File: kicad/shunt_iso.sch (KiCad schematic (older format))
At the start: 78 parts

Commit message: Come back to moldova to finish schematics and begin layout
I've started again from Moldova to discuss with Alexander the details.
I'm now working with schematics requeriments.
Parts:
- removed R?: 1M, symbol servo:Resistor
- added C? (x6): 100nF, symbol servo:Capacitor
- added C? (x2): 330p, symbol servo:Capacitor
- added J? (x2): Screw_Terminal_01x03, symbol Connector:Screw_Terminal_01x03
- added R? (x4): 1k, symbol servo:Resistor
- added R? (x4): 12e, symbol servo:Resistor
- added R?: 1M, symbol servo:Resistor
- added U? (x2): AMC1301, symbol servo:AMC1301
- added U? (x2): RFM-0505S, Converter_DCDC:C, symbol servo:RFM-0505S
- U: renamed from U?; value AMC1100 -> AMC1301; symbol servo:AMC1100 -> servo:AMC1301
- U?: value AMC1100 -> AMC1301; symbol servo:AMC1100 -> servo:AMC1301
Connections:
- net labels added: SHUNT_ISOA_ALLN, SHUNT_ISOA_ALLP, SHUNT_ISOB_ALLN, SHUNT_ISOB_ALLP
- wire segments 281 -> 361
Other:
- note added: "All"
- note added: "Measurement of A/B motor \nUVW phase current and A/B\nsum current, plus Vbus voltage"
- note added: "U"
- note added: "V"
- note added: "Vbus"
- note added: "W"
- note added: "with 3 screw connector you could choose\n3 range of current measurement to be at \n0.25v scale 1x, 2x or 4x.\n1-3 ------- X\n1-2 or 2-3 ------- 2X\n1-2 and 1-3 ------- 4X"
- moved on the sheet: C?, J?, R?, U?

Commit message: I've decided LEM lxs series, it's the best..
I've decided to use the LEM lxs, is a new series better than LTS and is
pin to pin compatible with the old one and also CAS series, so I think
it's a good option. 0.5usec rise time, multi prymari turns options, and
so..
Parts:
- removed C? (x20): 100nF, symbol servo:Capacitor
- removed C? (x4): 330p, symbol servo:Capacitor
- removed J? (x4): Screw_Terminal_01x03, symbol Connector:Screw_Terminal_01x03
- removed R? (x2): 1k, symbol servo:Resistor
- removed R? (x8): 12e, symbol servo:Resistor
- removed R? (x6): 20m, symbol servo:Resistor
- removed U (x3), U?: AMC1301, symbol servo:AMC1301
- removed U? (x8): RFM-0505S, Converter_DCDC:C, symbol servo:RFM-0505S
- added C? (x20): 100nF, symbol servo:Capacitor
- added C? (x9): 100n, symbol servo:C_Small
- added C? (x4): 330p, symbol servo:Capacitor
- added J? (x4): Screw_Terminal_01x03, symbol Connector:Screw_Terminal_01x03
- added L? (x18): L_Small, symbol servo:L_Small
- added R? (x18): 1k, symbol Device:R_Small
- added R? (x6): 20m, symbol servo:Resistor
- added R? (x8): 12e, symbol servo:Resistor
- added R? (x2): 1k, symbol servo:Resistor
- added U? (x8): RFM-0505S, Converter_DCDC:C, symbol servo:RFM-0505S
- added U? (x4): AMC1301, symbol servo:AMC1301
- renumbered U to U?
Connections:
- net 3V3: now also C?.2, C?.2, C?.2, C?.2, U?.1 (VDD1), U?.8 (VDD2), U?.8 (VDD2), U?.8 (VDD2)
- net GND: now also C?.1, C?.1, C?.1, C?.1, U?.4 (GND1), U?.5 (GND2), U?.5 (GND2), U?.5 (GND2)
- net GNDH: now also C?.1, C?.1, C?.1, C?.1, C?.1, C?.1, C?.1, C?.1, U?.1 (-VIN), U?.1 (-VIN), U?.1 (-VIN), U?.1 (-VIN), U?.1 (-VIN), U?.1 (-VIN), U?.1 (-VIN), U?.1 (-VIN)
- net SHUNT_ISOA_ALLN: now also C?.2, R?.2; no longer U?.6 (VOUT_N)
- net SHUNT_ISOA_ALLP: now also C?.1, R?.2; no longer U?.7 (VOUT_P)
- net SHUNT_ISOA_UN: now also C?.2, R?.2; no longer U?.6 (VOUT_N)
- net SHUNT_ISOA_UP: now also C?.1, R?.2; no longer U?.7 (VOUT_P)
- net SHUNT_ISOA_VN: now also C?.2, R?.2; no longer U?.6 (VOUT_N)
- net SHUNT_ISOA_VP: now also C?.1, R?.2; no longer U?.7 (VOUT_P)
- net SHUNT_ISOA_WN: now also C?.2, R?.2; no longer U?.3 (VIN_N)
- net SHUNT_ISOA_WP: now also C?.1, R?.2; no longer U?.2 (VIN_P)
- net SHUNT_ISOB_ALLN: now also C?.2, R?.2
- net SHUNT_ISOB_ALLP: now also C?.1, R?.2
- net SHUNT_ISOB_UN: now also C?.2, R?.2
- net SHUNT_ISOB_UP: now also C?.1, R?.2
- net SHUNT_ISOB_VN: now also C?.2, R?.2
- net SHUNT_ISOB_VP: now also C?.1, R?.2
- net SHUNT_ISOB_WN: now also C?.2, R?.2
- net SHUNT_ISOB_WP: now also C?.1, R?.2
- net SHUNT_ISO_BUSN: now also C?.2, R?.2; no longer U?.6 (VOUT_N)
- net SHUNT_ISO_BUSP: now also C?.1, R?.2; no longer U?.7 (VOUT_P)
- net at C?.2, U?.1 (VDD1): now also L?.1; no longer U?.4 (+VOUT)
- net at U?.1 (VDD1): now also C?.2, L?.1 (x3)
- net at C?.1, R?.1, U?.3 (VIN_N)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: now also C?.1, U?.3 (-VOUT) (x3)
- net at C?.1, R?.1, U?.5 (GND2)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: now also C?.1, U?.3 (-VOUT)
- net at U?.8 (VDD2): now also C?.2, L?.1
- net 15VH: no longer names the net of C?.2, U?.2 (+VIN)
- net 15VH: now also L?.2
- new net: R?.1, U?.6 (VOUT_N) (x7)
- new net: R?.1, U?.7 (VOUT_P) (x7)
- new net: L?.2, U?.4 (+VOUT) (x9)
- new net: R?.1, U?.2 (VIN_P) (x2)
- new net: R?.1, U?.3 (VIN_N) (x2)
- new net: C?.2, L?.2, U?.2 (+VIN) (x8)
- new net: C?.2, L?.1, U?.1 (VDD1) (x3)
- new net: C?.2, R?.1, U?.2 (VIN_P) (x3)
- new net: C?.1, C?.1, R?.1, U?.3 (-VOUT), U?.3 (VIN_N), U?.4 (GND1) (x3)
- new net: J?.2 (Pin_2), R?.1, R?.2 (x4)
- new net: J?.1 (Pin_1), R?.2, R?.2 (x4)
- new net: J?.3 (Pin_3), R?.1, R?.2 (x4)
- new net: C?.1, C?.1, R?.1, U?.3 (-VOUT), U?.5 (GND2), U?.6 (VOUT_N)
- new net: C?.2, R?.1, U?.7 (VOUT_P)
- new net: C?.2, L?.1, U?.8 (VDD2)
- new net 5VH: L?.1, L?.1, L?.1, L?.1, L?.1, L?.1, L?.1, L?.1, L?.1
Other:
- note added: "Current of 3 phases +\nsum current +\nVbus voltage"
- note added: "SHUT -> ADC -> SD -> DAC\n"
- note added: "divider to measure Vbus"
- note removed: "Measurement of A/B motor \nUVW phase current and A/B\nsum current, plus Vbus voltage"
- moved on the sheet: C?, J?, R?, U?

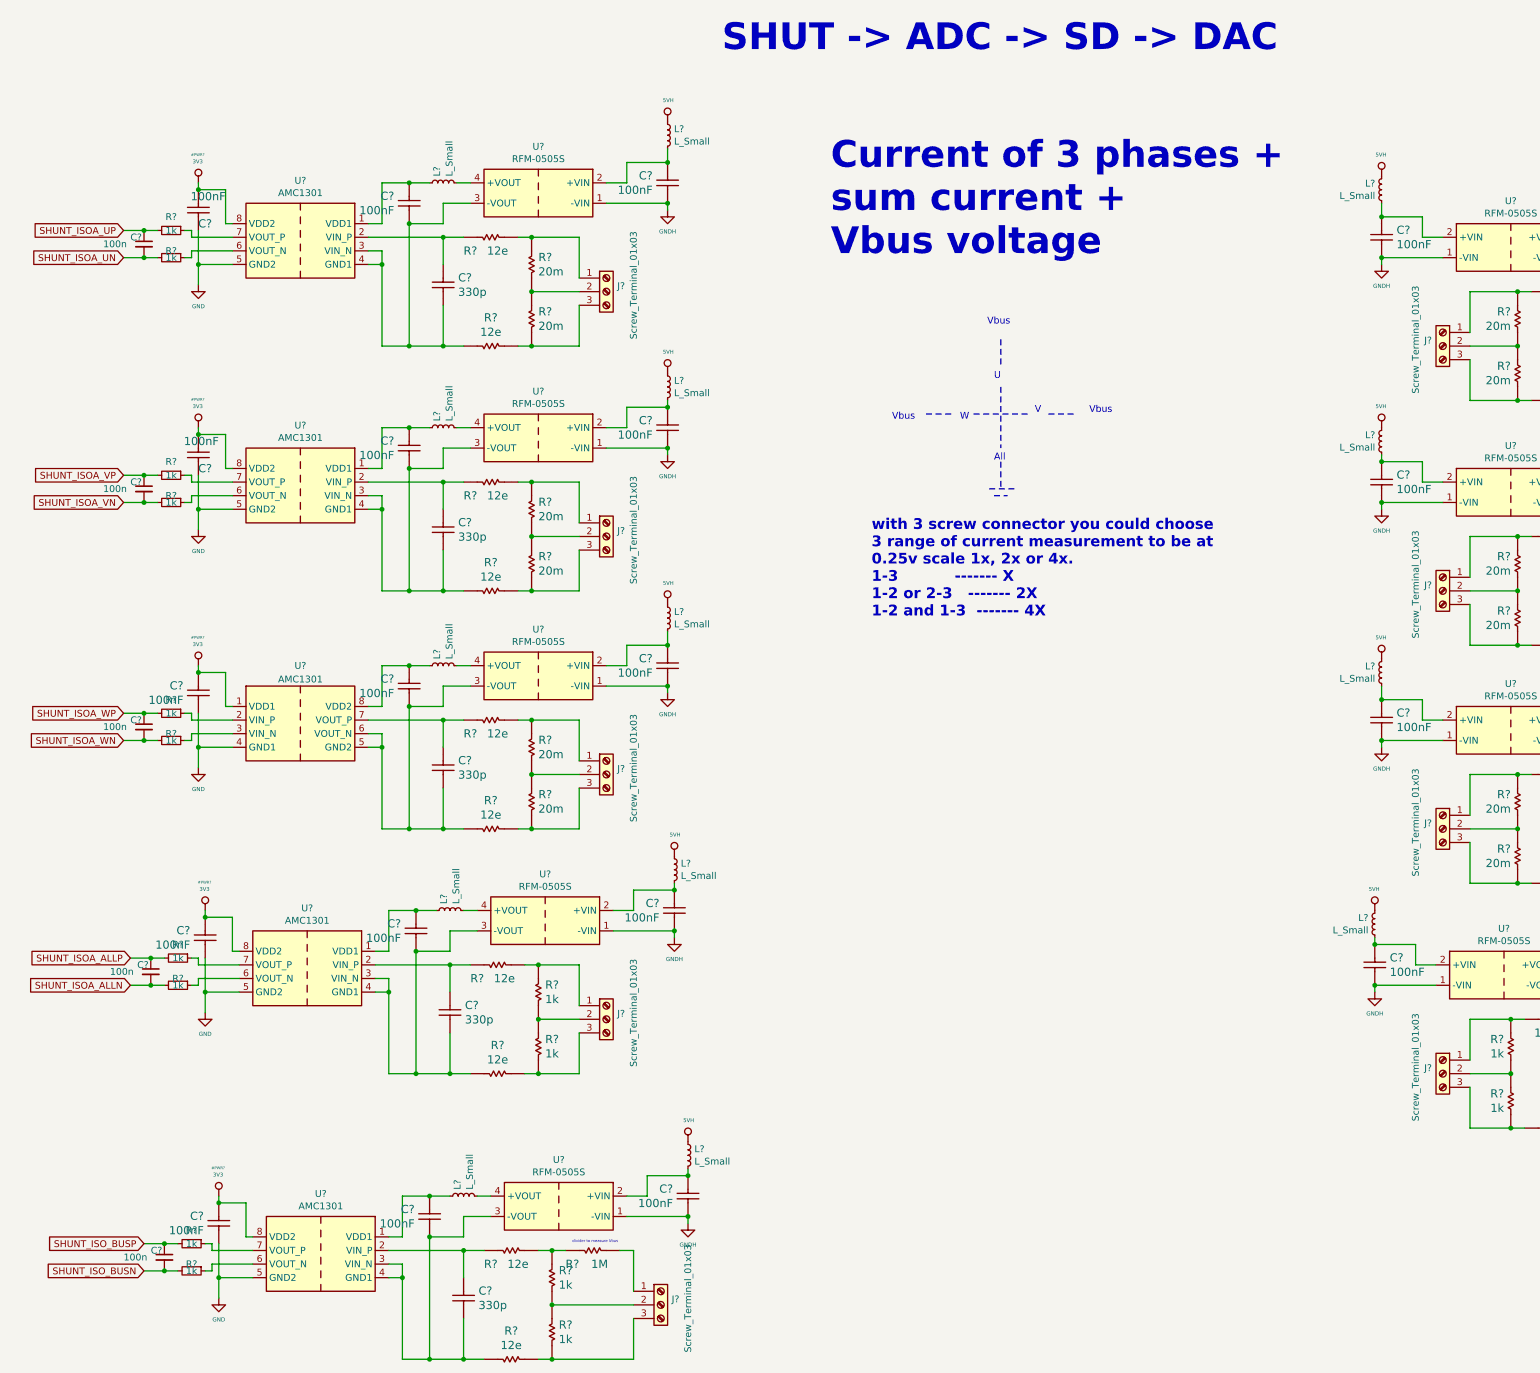
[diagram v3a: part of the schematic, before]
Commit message: I've added LCD UI interfase, EQEP and finish ENDAT
I think I have almos all the interfases ready, I'm begining the
verigication process and then the part definig
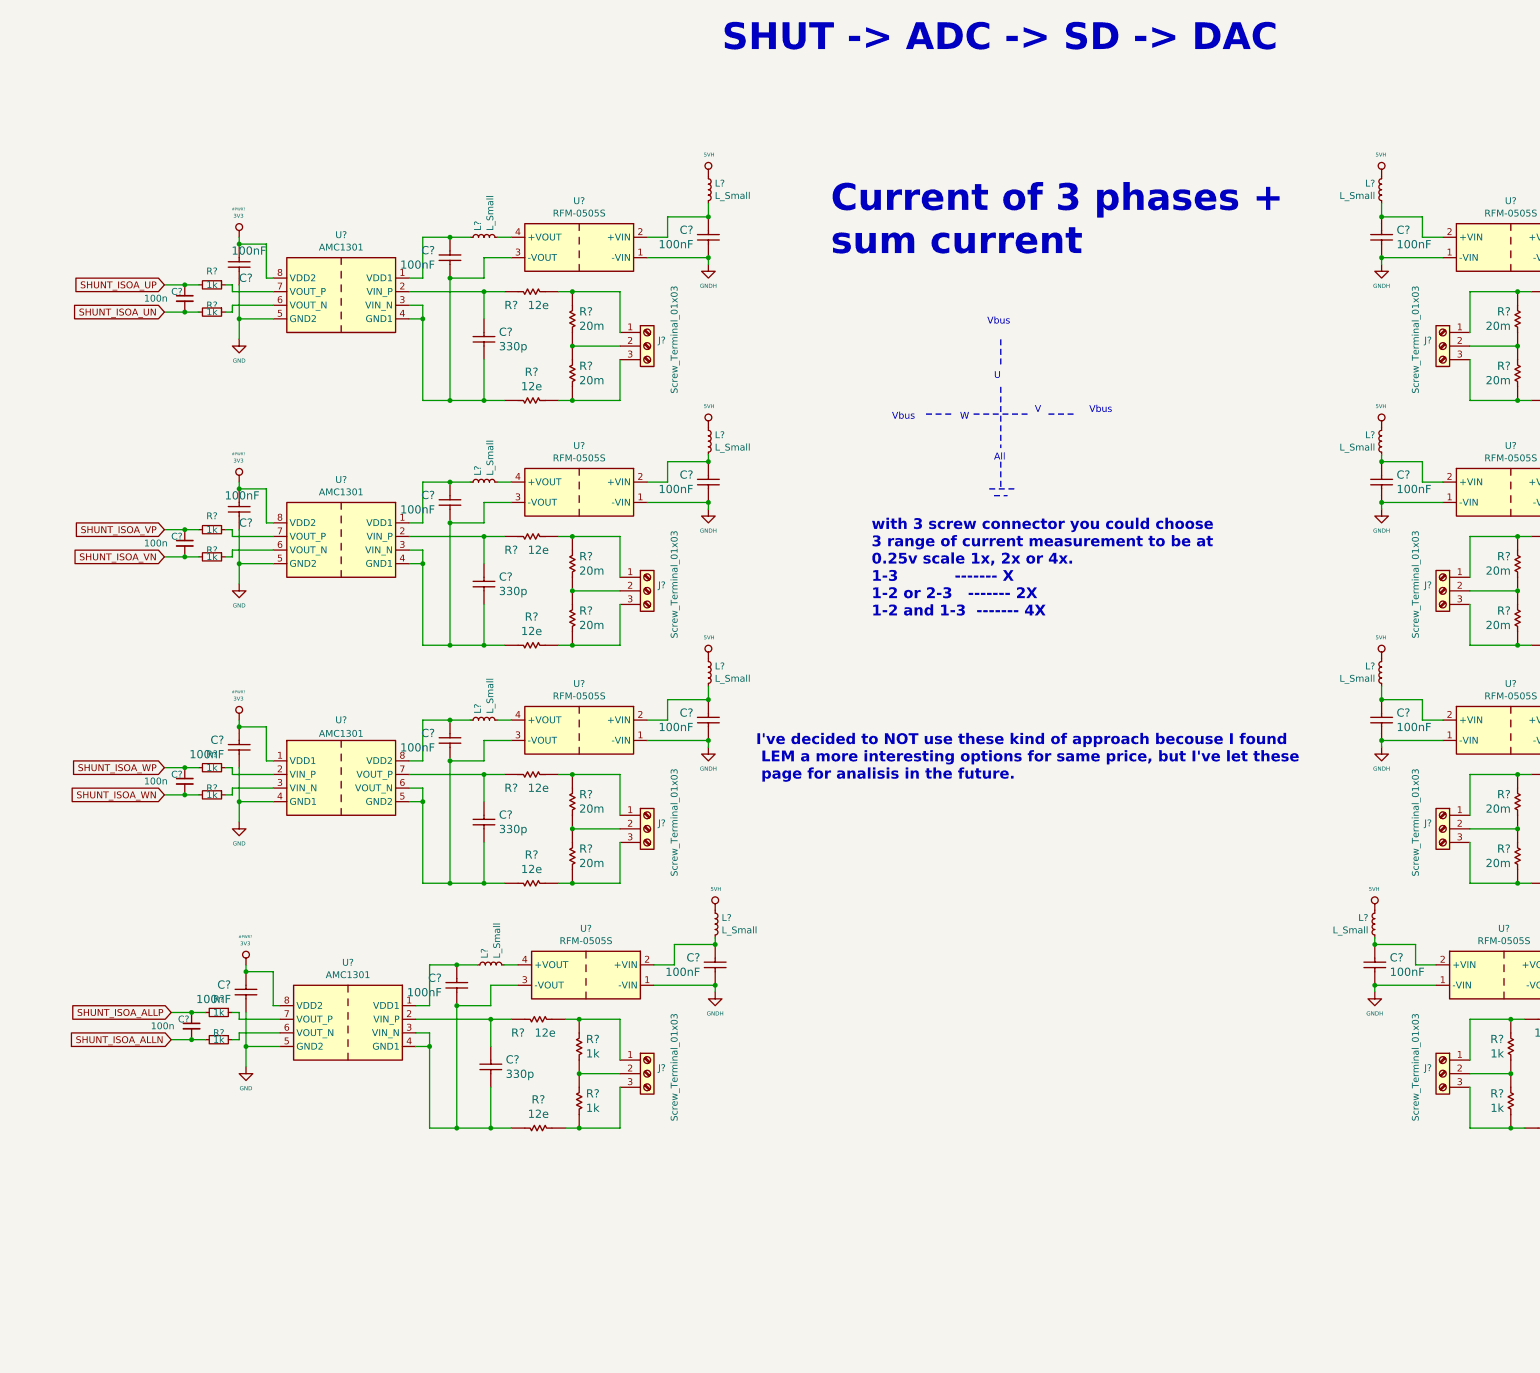
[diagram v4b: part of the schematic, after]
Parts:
- removed C? (x3): 100nF, symbol servo:Capacitor
- removed C?: 330p, symbol servo:Capacitor
- removed C?: 100n, symbol servo:C_Small
- removed J?: Screw_Terminal_01x03, symbol Connector:Screw_Terminal_01x03
- removed L? (x2): L_Small, symbol servo:L_Small
- removed R? (x2): 1k, symbol servo:Resistor
- removed R? (x2): 12e, symbol servo:Resistor
- removed R?: 1M, symbol servo:Resistor
- removed R? (x2): 1k, symbol Device:R_Small
- removed U?: AMC1301, symbol servo:AMC1301
- removed U?: RFM-0505S, Converter_DCDC:C, symbol servo:RFM-0505S
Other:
- note added: "Current of 3 phases +\nsum current"
- note added: "I've decided to NOT use these kind of approach becouse I found\n LEM a more interesting options for same price, but I've let these\n page for analisis in the future."
- note removed: "Current of 3 phases +\nsum current +\nVbus voltage"
- note removed: "divider to measure Vbus"
- moved on the sheet: C?, J?, L?, R?, U?
